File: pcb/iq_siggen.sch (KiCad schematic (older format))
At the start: 114 parts, among them J1 J3 - BANK0, J10 Barrel_Jack_MountingPin, J11 Conn_Coaxial, J12 Conn_01x01_Male, J13 Conn_01x01_Male, J14 Conn_01x01_Male, J15 Conn_01x01_Male, J16 Conn_01x01_Male, J17 Conn_01x01_Male, J2 J4 - BANK1, J3 Conn_01x20_Male, J4 Conn_01x01_Male, J6 Conn_Coaxial, J7 Conn_Coaxial, J8 Conn_Coaxial, J9 Conn_Coaxial, SW1 SW_Push, SW2 SW_Push, SW3 SW_Push, SW4 SW_Push, U1 AMS1117-3.3, U2 TPS72325DBVR, U3 TLV73325PDBVT

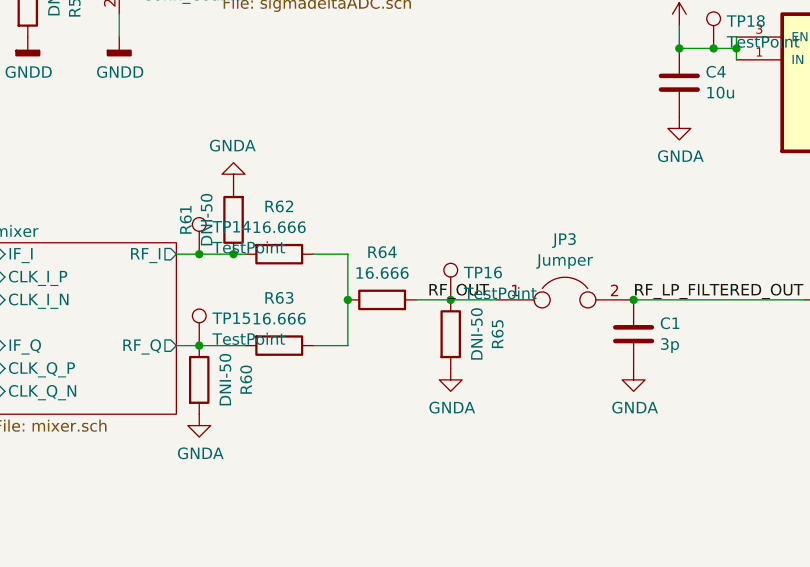
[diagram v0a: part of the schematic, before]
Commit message: clean up LO driver routing
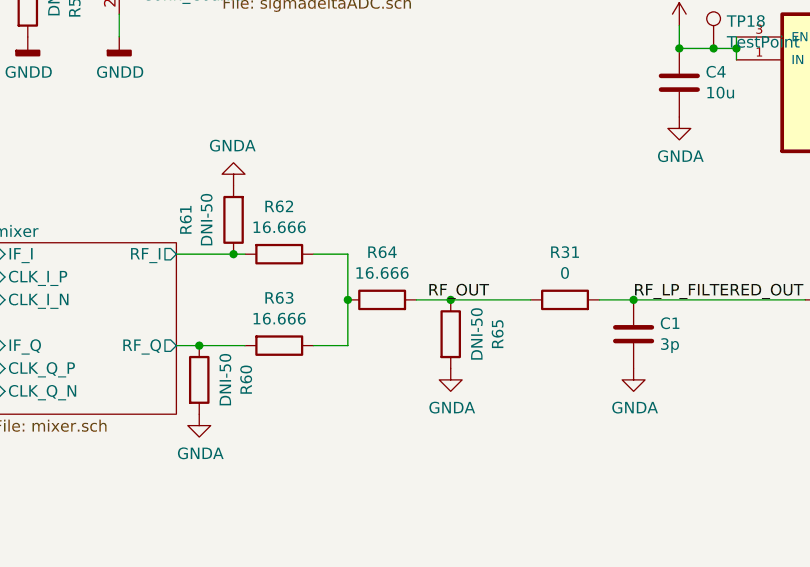
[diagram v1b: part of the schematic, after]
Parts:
- removed JP3: Jumper, symbol Device:Jumper
- removed TP14, TP15, TP16: TestPoint, TestPoint:TestPoint_Pad_D1.5mm, symbol Connector:TestPoint
- added R31: 0, Resistor_SMD:R_0603_1608Metric, symbol Device:R
- J11: footprint Connector_Coaxial:SMA_Samtec_SMA-J-P-X-ST-EM1_EdgeMount -> iq_siggen:SMA_Samtec_SMA-J-P-X-ST-EM1_EdgeMount_withSTEP
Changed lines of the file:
@@
 	5750 5950 6150 5950
-Wire Wire Line
-	6950 5550 7050 5550
 Wire Wire Line
 	7250 5950 7050 5950
@@
 F 0 "J11" H 10000 5725 50  0000 L CNN
 F 1 "Conn_Coaxial" H 10000 5634 50  0000 L CNN
-F 2 "Connector_Coaxial:SMA_Samtec_SMA-J-P-X-ST-EM1_EdgeMount" H 9900 5750 50  0001 C CNN
+F 2 "iq_siggen:SMA_Samtec_SMA-J-P-X-ST-EM1_EdgeMount_withSTEP" H 9900 5750 50  0001 C CNN
 F 3 " ~" H 9900 5750 50  0001 C CNN
 	1    9900 5750
@@
 F 3 "" H 9900 5950 50  0001 C CNN
 	1    9900 5950
-	1    0    0    -1
-$EndComp
-$Comp
-L Connector:TestPoint TP14
-U 1 1 5FD7CA10
-P 7050 5550
-F 0 "TP14" H 7108 5668 50  0000 L CNN
-F 1 "TestPoint" H 7108 5577 50  0000 L CNN
-F 2 "TestPoint:TestPoint_Pad_D1.5mm" H 7250 5550 50  0001 C CNN
-F 3 "~" H 7250 5550 50  0001 C CNN
-	1    7050 5550
-	1    0    0    -1
-$EndComp
-Connection ~ 7050 5550
-Wire Wire Line
-	7050 5550 7200 5550
-$Comp
-L Connector:TestPoint TP15
-U 1 1 5FD7CF01
-P 7050 5950
-F 0 "TP15" H 7108 6068 50  0000 L CNN
-F 1 "TestPoint" H 7108 5977 50  0000 L CNN
-F 2 "TestPoint:TestPoint_Pad_D1.5mm" H 7250 5950 50  0001 C CNN
-F 3 "~" H 7250 5950 50  0001 C CNN
-	1    7050 5950
 	1    0    0    -1
 $EndComp
@@
 Wire Wire Line
 	3050 5900 2600 5900
-$Comp
-L Device:Jumper JP3
-U 1 1 6050A1A3
-P 8650 5750
-F 0 "JP3" H 8650 6014 50  0000 C CNN
-F 1 "Jumper" H 8650 5923 50  0000 C CNN
-F 2 "" H 8650 5750 50  0001 C CNN
-F 3 "~" H 8650 5750 50  0001 C CNN
-	1    8650 5750
-	1    0    0    -1
-$EndComp
 Wire Wire Line
 	8950 5750 9700 5750
@@
 $EndComp
 Connection ~ 8150 5750
-Wire Wire Line
-	8150 5750 8350 5750
 $Comp
 L power:GNDA #PWR022
@@
 	2600 5900 2400 5900
 $Comp
-L Connector:TestPoint TP16
-U 1 1 609BA25B
-P 8150 5750
-F 0 "TP16" H 8208 5868 50  0000 L CNN
-F 1 "TestPoint" H 8208 5777 50  0000 L CNN
-F 2 "TestPoint:TestPoint_Pad_D1.5mm" H 8350 5750 50  0001 C CNN
-F 3 "~" H 8350 5750 50  0001 C CNN
-	1    8150 5750
-	1    0    0    -1
-$EndComp
-$Comp
 L Connector:TestPoint TP22
 U 1 1 609C89DC
@@
 	1    0    0    -1
 $EndComp
-Connection ~ 8950 5750
 $Comp
 L power:GNDA #PWR026
@@
 	0    -1   -1   0
 $EndComp
-Wire Bus Line
-	2500 3650 2500 5500
-Wire Bus Line
-	2950 3650 2950 5400
 $Comp
 L Device:R R8
@@
 	-1   0    0    1
 $EndComp
+Wire Wire Line
+	6950 5550 7200 5550
+$Comp
+L Device:R R31
+U 1 1 5FC7FB3D
+P 8650 5750
+F 0 "R31" V 8857 5750 50  0000 C CNN
+F 1 "0" V 8766 5750 50  0000 C CNN
+F 2 "Resistor_SMD:R_0603_1608Metric" V 8580 5750 50  0001 C CNN
+F 3 "~" H 8650 5750 50  0001 C CNN
+	1    8650 5750
+	0    -1   -1   0
+$EndComp
+Wire Wire Line
+	8800 5750 8950 5750
+Connection ~ 8950 5750
+Wire Wire Line
+	8150 5750 8500 5750
+Wire Bus Line
+	2500 3650 2500 5500
+Wire Bus Line
+	2950 3650 2950 5400
 $EndSCHEMATC

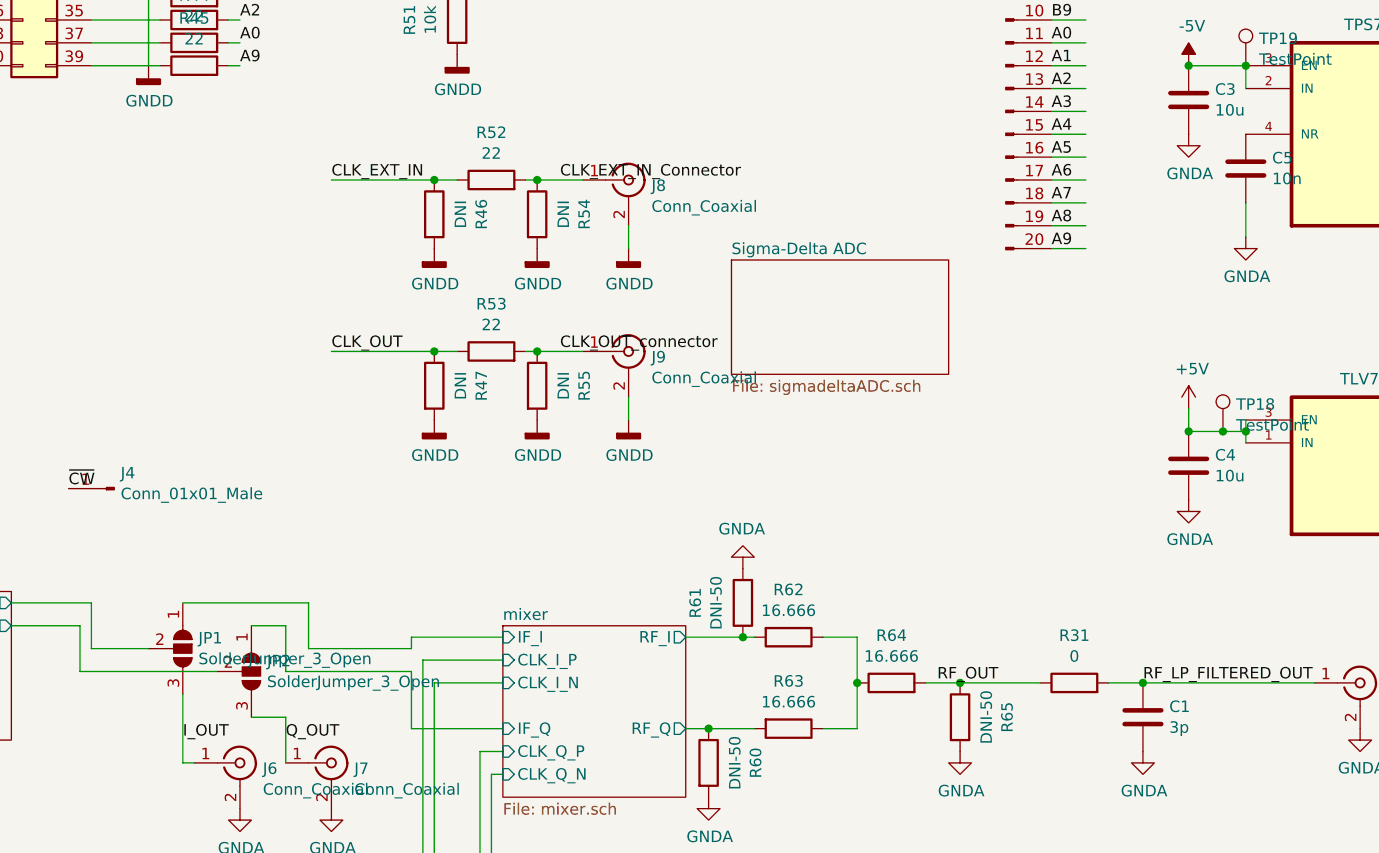
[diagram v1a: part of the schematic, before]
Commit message: route power for amplifiers, fill zones for gnd and amplifiers
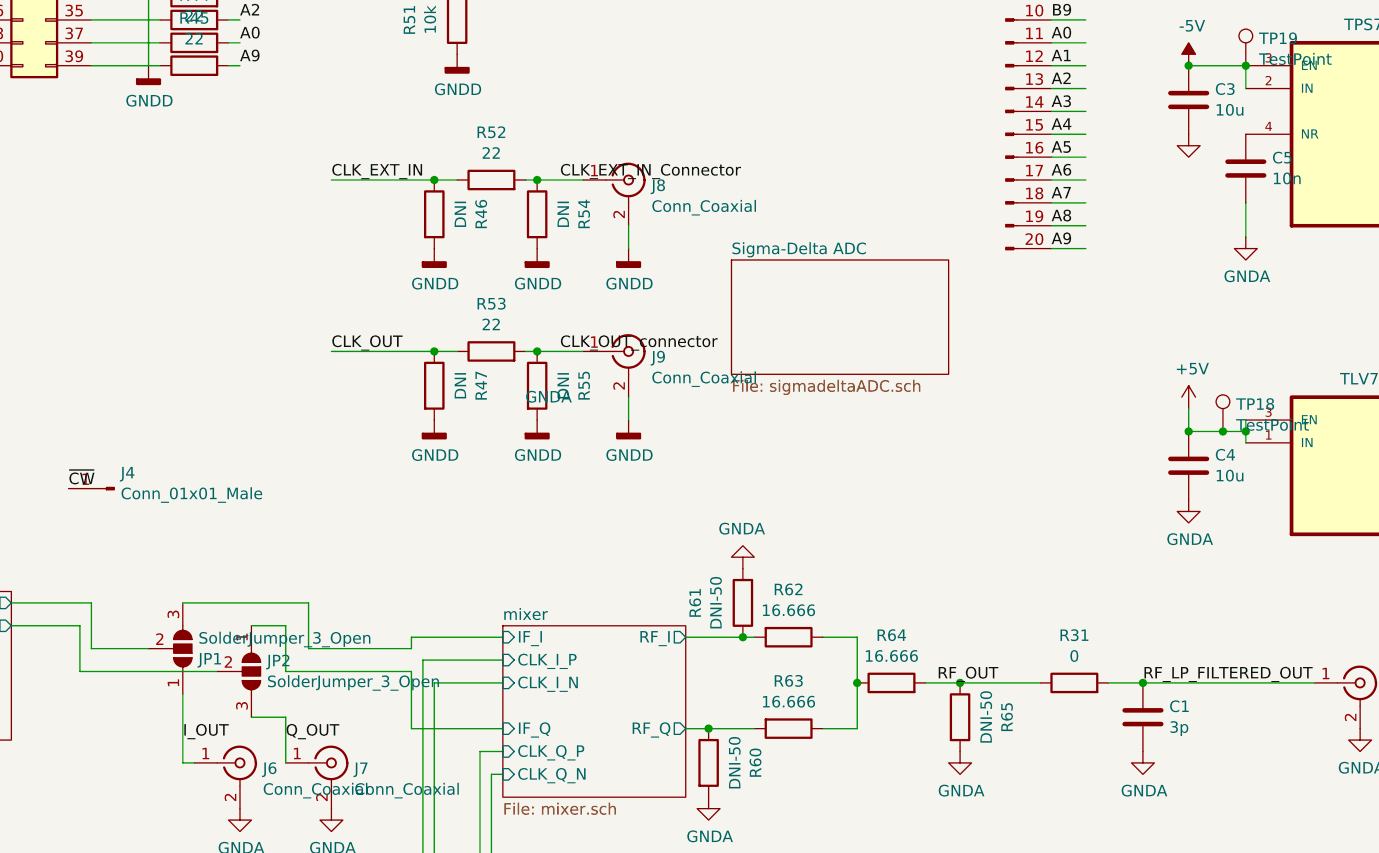
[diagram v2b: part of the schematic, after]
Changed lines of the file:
@@
 P 9150 3350
 F 0 "#PWR028" H 9150 3100 50  0001 C CNN
-F 1 "GNDA" H 9155 3177 50  0000 C CNN
+F 1 "GNDA" H 6350 2200 50  0000 C CNN
 F 2 "" H 9150 3350 50  0001 C CNN
 F 3 "" H 9150 3350 50  0001 C CNN
@@
 F 3 "~" H 4750 5600 50  0001 C CNN
 	1    4750 5600
-	0    1    1    0
-$EndComp
-$Comp
+	0    1    -1   0
+$EndComp
+$Comp

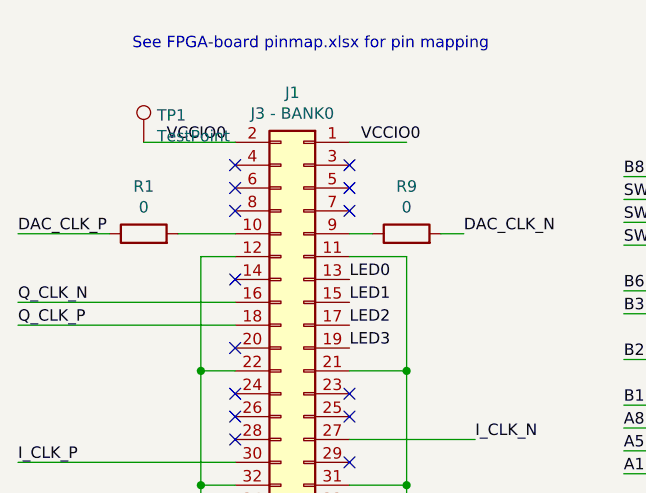
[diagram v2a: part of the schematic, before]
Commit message: routing the dac wires
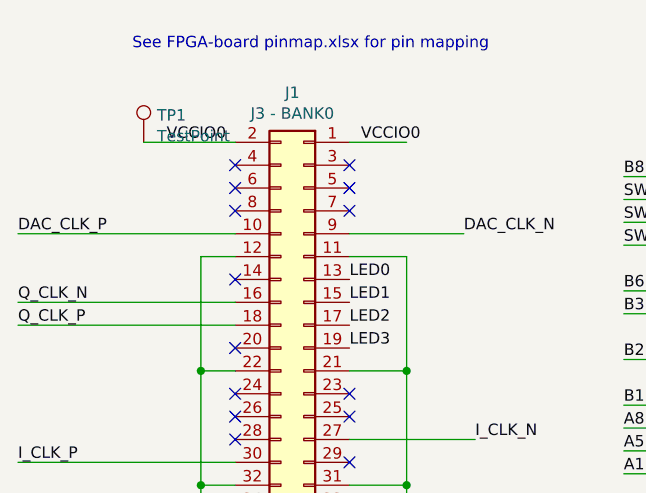
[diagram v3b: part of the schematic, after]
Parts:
- removed R1, R9: 0, Resistor_SMD:R_0603_1608Metric, symbol Device:R
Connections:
- wire segments 275 -> 273
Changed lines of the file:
@@
 	3800 6700 3800 6850
-Wire Wire Line
-	1450 1500 1200 1500
-Wire Wire Line
-	2450 1500 2350 1500
 Wire Wire Line
 	3800 6600 5800 6600
@@
 Wire Wire Line
 	5950 950  6000 950
-$Comp
-L Device:R R9
-U 1 1 6062FA4E
-P 2200 1500
-F 0 "R9" V 2407 1500 50  0000 C CNN
-F 1 "0" V 2316 1500 50  0000 C CNN
-F 2 "Resistor_SMD:R_0603_1608Metric" V 2130 1500 50  0001 C CNN
-F 3 "~" H 2200 1500 50  0001 C CNN
-	1    2200 1500
-	0    -1   -1   0
-$EndComp
-Wire Wire Line
-	2050 1500 1950 1500
-$Comp
-L Device:R R1
-U 1 1 6065D95A
-P 1050 1500
-F 0 "R1" V 1257 1500 50  0000 C CNN
-F 1 "0" V 1166 1500 50  0000 C CNN
-F 2 "Resistor_SMD:R_0603_1608Metric" V 980 1500 50  0001 C CNN
-F 3 "~" H 1050 1500 50  0001 C CNN
-	1    1050 1500
-	0    -1   -1   0
-$EndComp
-Wire Wire Line
-	900  1500 500  1500
 $Comp
 L Device:R R17
@@
 Wire Wire Line
 	8150 5750 8500 5750
+Wire Wire Line
+	1950 1500 2450 1500
+Wire Wire Line
+	500  1500 1450 1500
 Wire Bus Line
 	2500 3650 2500 5500

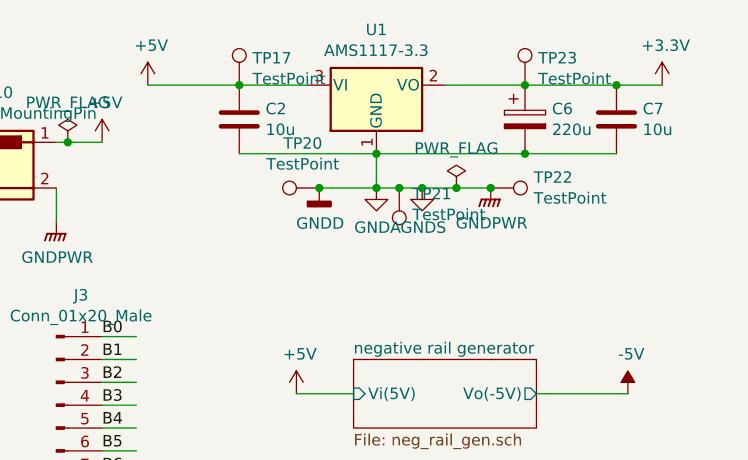
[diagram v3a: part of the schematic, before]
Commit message: laying out split gnd pours
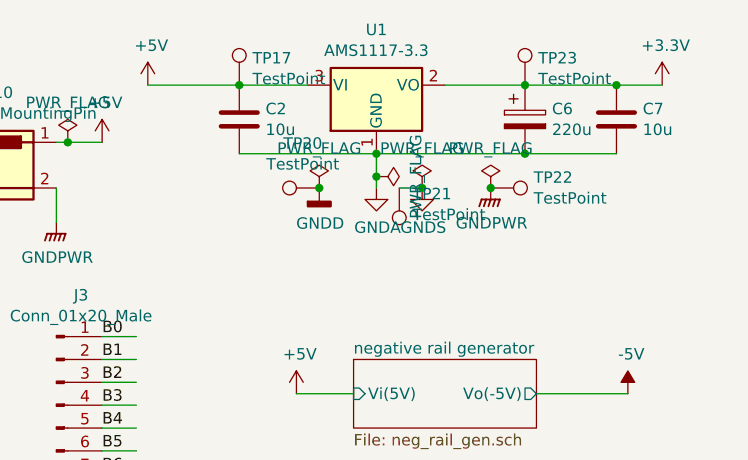
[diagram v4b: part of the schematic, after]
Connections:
- wire segments 273 -> 270
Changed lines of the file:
@@
 	11000 850  10800 850
-$Comp
-L power:GNDA #PWR034
-U 1 1 5F74AAE8
-P 9750 1300
-F 0 "#PWR034" H 9750 1050 50  0001 C CNN
-F 1 "GNDA" H 9755 1127 50  0000 C CNN
-F 2 "" H 9750 1300 50  0001 C CNN
-F 3 "" H 9750 1300 50  0001 C CNN
-	1    9750 1300
-	1    0    0    -1
-$EndComp
 $Comp
 L power:GNDS #PWR036
@@
 Wire Wire Line
 	9950 1300 9850 1300
-Connection ~ 9750 1300
-Wire Wire Line
-	9750 1300 9500 1300
-Wire Wire Line
-	9750 1150 9750 1300
+Wire Wire Line
+	9750 1150 9750 1250
 $Comp
 L power:+5V #PWR025
@@
 	1    0    0    -1
 $EndComp
-Wire Wire Line
-	10250 1300 10100 1300
-Connection ~ 9950 1300
 $Comp
 L TPS72325DBVR:TPS72325DBVR U2
@@
 L power:PWR_FLAG #FLG02
 U 1 1 5FE3A2C2
-P 10100 1300
-F 0 "#FLG02" H 10100 1375 50  0001 C CNN
-F 1 "PWR_FLAG" H 10100 1473 50  0000 C CNN
-F 2 "" H 10100 1300 50  0001 C CNN
-F 3 "~" H 10100 1300 50  0001 C CNN
-	1    10100 1300
-	1    0    0    -1
-$EndComp
-Connection ~ 10100 1300
-Wire Wire Line
-	10100 1300 9950 1300
+P 10250 1300
+F 0 "#FLG02" H 10250 1375 50  0001 C CNN
+F 1 "PWR_FLAG" H 10250 1473 50  0000 C CNN
+F 2 "" H 10250 1300 50  0001 C CNN
+F 3 "~" H 10250 1300 50  0001 C CNN
+	1    10250 1300
+	1    0    0    -1
+$EndComp
 Wire Wire Line
 	6150 5650 5800 5650
@@
 	0    1    1    0
 $EndComp
-Connection ~ 10250 1300
 $Comp
 L Connector:TestPoint TP20
@@
 	0    -1   -1   0
 $EndComp
-Connection ~ 9500 1300
 $Comp
 L Connector:TestPoint TP21
@@
 	-1   0    0    1
 $EndComp
-Connection ~ 9850 1300
-Wire Wire Line
-	9850 1300 9750 1300
 $Comp
 L Connector:TestPoint TP17
@@
 Wire Wire Line
 	500  1500 1450 1500
+$Comp
+L power:GNDA #PWR034
+U 1 1 5F74AAE8
+P 9750 1300
+F 0 "#PWR034" H 9750 1050 50  0001 C CNN
+F 1 "GNDA" H 9755 1127 50  0000 C CNN
+F 2 "" H 9750 1300 50  0001 C CNN
+F 3 "" H 9750 1300 50  0001 C CNN
+	1    9750 1300
+	1    0    0    -1
+$EndComp
+Connection ~ 10250 1300
 Wire Bus Line
 	2500 3650 2500 5500
 Wire Bus Line
 	2950 3650 2950 5400
+$Comp
+L power:PWR_FLAG #FLG0101
+U 1 1 5FC86BBE
+P 9950 1300
+F 0 "#FLG0101" H 9950 1375 50  0001 C CNN
+F 1 "PWR_FLAG" H 9950 1473 50  0000 C CNN
+F 2 "" H 9950 1300 50  0001 C CNN
+F 3 "~" H 9950 1300 50  0001 C CNN
+	1    9950 1300
+	1    0    0    -1
+$EndComp
+Connection ~ 9950 1300
+$Comp
+L power:PWR_FLAG #FLG0102
+U 1 1 5FC86DEB
+P 9500 1300
+F 0 "#FLG0102" H 9500 1375 50  0001 C CNN
+F 1 "PWR_FLAG" H 9500 1473 50  0000 C CNN
+F 2 "" H 9500 1300 50  0001 C CNN
+F 3 "~" H 9500 1300 50  0001 C CNN
+	1    9500 1300
+	1    0    0    -1
+$EndComp
+Connection ~ 9500 1300
+$Comp
+L power:PWR_FLAG #FLG0103
+U 1 1 5FC87182
+P 9750 1250
+F 0 "#FLG0103" H 9750 1325 50  0001 C CNN
+F 1 "PWR_FLAG" H 9750 1423 50  0000 C CNN
+F 2 "" H 9750 1250 50  0001 C CNN
+F 3 "~" H 9750 1250 50  0001 C CNN
+	1    9750 1250
+	0    1    1    0
+$EndComp
+Connection ~ 9750 1250
+Wire Wire Line
+	9750 1250 9750 1300
 $EndSCHEMATC
